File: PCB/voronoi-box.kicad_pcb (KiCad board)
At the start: 2 copper layers, 16 parts, among them J1 Conn_01x02_Male, J2 Conn_01x02_Male, J3 Conn_01x03_Female, SW1 SW_Push, SW2 SW_Push, U1 ATtiny85-20PU

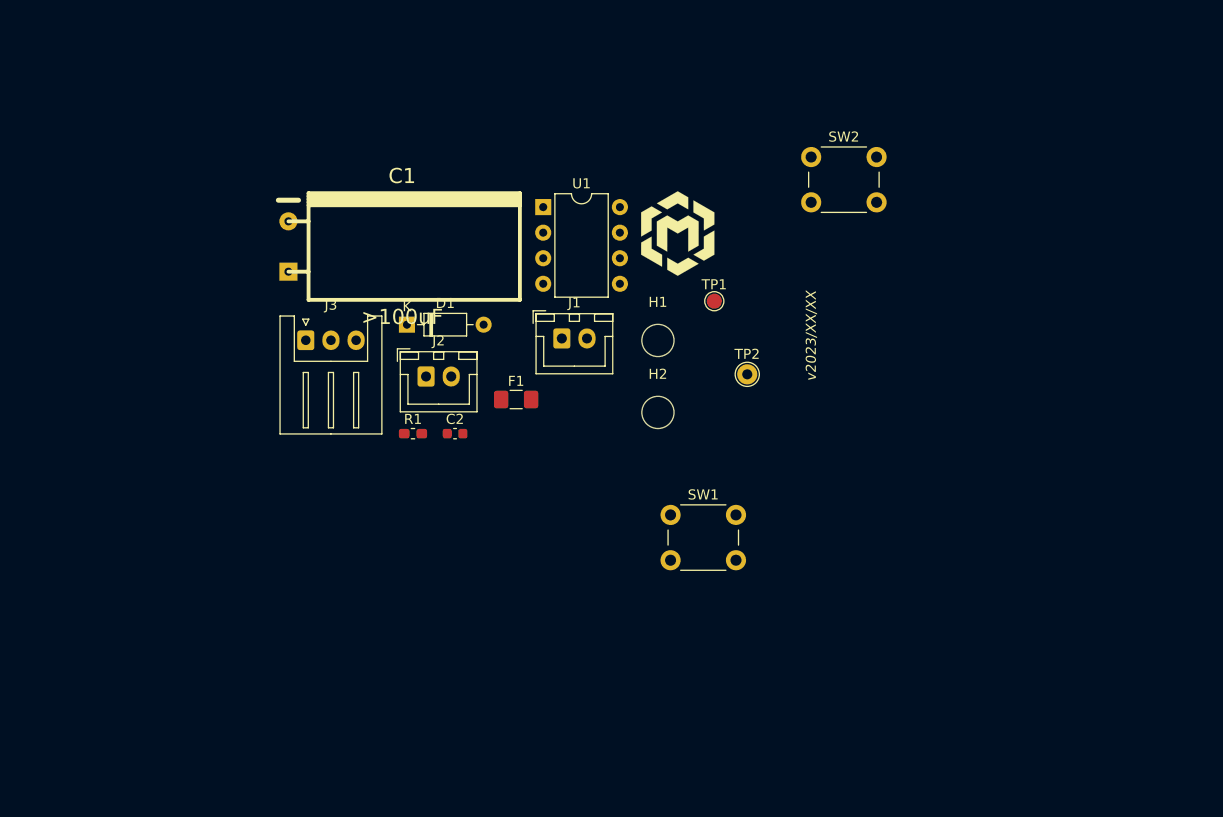
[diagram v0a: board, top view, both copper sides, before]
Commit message: extend Readme with a huge knowledge drop, create new power path with dedicated parts, add ISP, use analog mux for buttons, try to fix CI
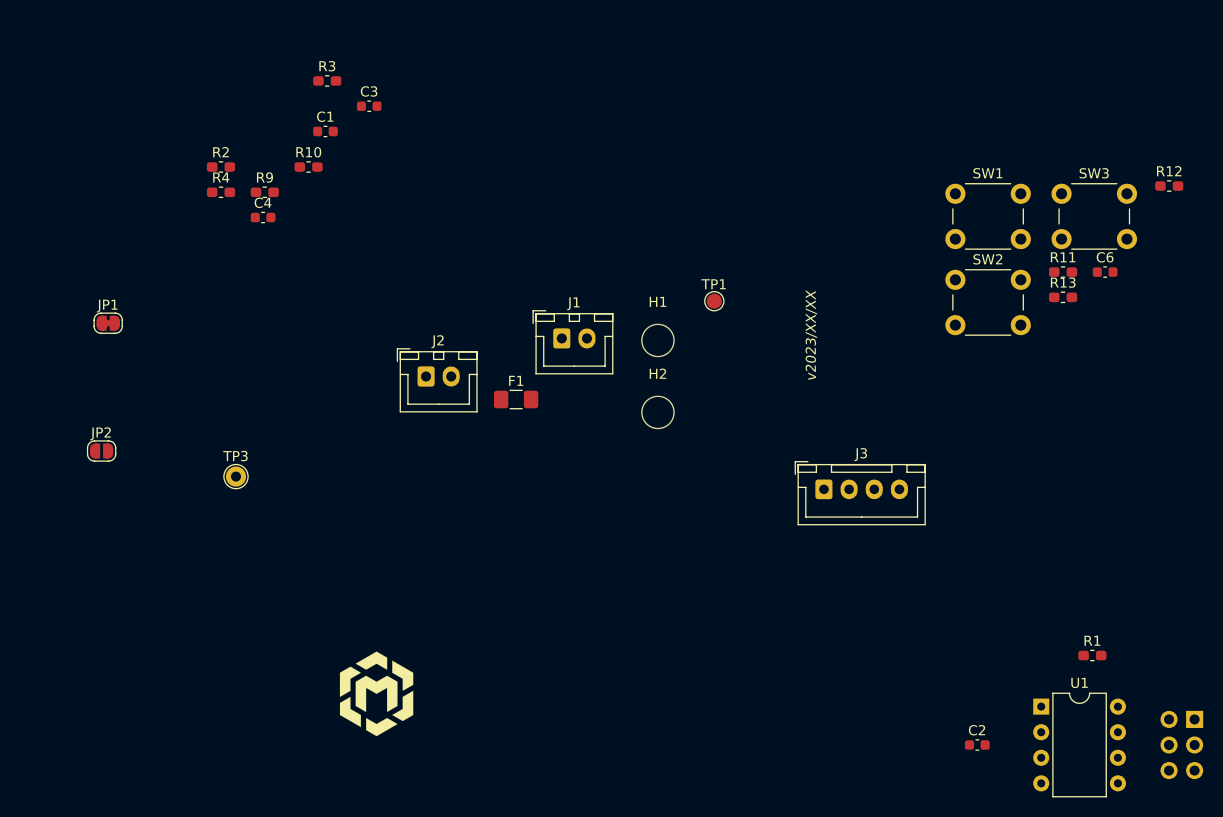
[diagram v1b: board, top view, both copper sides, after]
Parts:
- removed D1: D, Diode_THT:D_DO-35_SOD27_P7.62mm_Horizontal
- removed TP2: RESERVE, TestPoint:TestPoint_THTPad_D2.0mm_Drill1.0mm
- added C3: 1uF, Capacitor_SMD:C_0603_1608Metric, F.Cu at (43.7, 21.6)
- added C4: 100nF, Capacitor_SMD:C_0603_1608Metric, F.Cu at (33.2, 32.7)
- added C6: 100nF, Capacitor_SMD:C_0603_1608Metric, F.Cu at (116.8, 38.1)
- added J4: AVR-ISP-6, Connector_PinHeader_2.54mm:PinHeader_2x03_P2.54mm_Vertical, B.Cu at (125.7, 82.5)
- added JP1: Cut for NTC, Jumper:SolderJumper-2_P1.3mm_Bridged_RoundedPad1.0x1.5mm, F.Cu at (17.8, 43.2)
- added JP2: Join without BMS, Jumper:SolderJumper-2_P1.3mm_Open_RoundedPad1.0x1.5mm, F.Cu at (17.1, 55.9)
- added R10: 1k, Resistor_SMD:R_0603_1608Metric_Pad1.05x0.95mm_HandSolder, F.Cu at (37.7, 27.7)
- added R11: 1k, Resistor_SMD:R_0603_1608Metric_Pad1.05x0.95mm_HandSolder, F.Cu at (112.7, 38.1)
- added R12: 2.2k, Resistor_SMD:R_0603_1608Metric_Pad1.05x0.95mm_HandSolder, F.Cu at (123.2, 29.6)
- added R13: 4.7k, Resistor_SMD:R_0603_1608Metric_Pad1.05x0.95mm_HandSolder, F.Cu at (112.7, 40.6)
- added R2: 2k, Resistor_SMD:R_0603_1608Metric_Pad1.05x0.95mm_HandSolder, F.Cu at (29.0, 27.7)
- added R3: 1.5k, Resistor_SMD:R_0603_1608Metric_Pad1.05x0.95mm_HandSolder, F.Cu at (39.5, 19.1)
- added R4: 10k, Resistor_SMD:R_0603_1608Metric_Pad1.05x0.95mm_HandSolder, F.Cu at (29.0, 30.2)
- added R9: 47k, Resistor_SMD:R_0603_1608Metric_Pad1.05x0.95mm_HandSolder, F.Cu at (33.3, 30.2)
- added SW3: SW_3, Button_Switch_THT:SW_PUSH_6mm_H4.3mm, F.Cu at (112.5, 30.3)
- added TP3: TEMP, TestPoint:TestPoint_THTPad_D2.0mm_Drill1.0mm, F.Cu at (30.5, 58.4)
- C1: value >100uF -> 1uF; footprint w_capacitors:CP_10x20mm_hor -> Capacitor_SMD:C_0603_1608Metric
- J1: value Conn_01x02_Male -> LiPo (1S/3.7V)
- J2: value Conn_01x02_Male -> USB/PWR
- J3: value Conn_01x03_Female -> LEDs; footprint Connector_JST:JST_XH_S3B-XH-A_1x03_P2.50mm_Horizontal -> Connector_JST:JST_XH_B4B-XH-A_1x04_P2.50mm_Vertical
- R1: value 10k -> 4.7k
- SW1: value SW_Push -> SW_1
- SW2: value SW_Push -> SW_2
- moved R1 71.0 mm to (115.6, 76.2)
- moved U1 70.1 mm to (110.5, 81.3)
- moved C2 60.4 mm to (104.1, 85.1)
- moved L1 54.7 mm to (44.5, 80.0)
- moved J3 53.6 mm to (88.9, 59.7)
- moved SW1 42.7 mm to (102.0, 30.3)
- moved SW2 18.8 mm to (102.0, 38.9)
- moved C1 13.7 mm to (39.4, 24.1)
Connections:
- net Net-(R1-Pad2) renamed /RESET
- net Net-(TP1-Pad1) renamed /AREF
- C1 pad 1: VCC -> VBUS
- F1 pad 1: (no net) -> VBUS
- F1 pad 2: VBUS -> Net-(F1-Pad2)
- J1 pad 1: (no net) -> +BATT
- J1 pad 2: GND -> -BATT
- J2 pad 1: VBUS -> Net-(F1-Pad2)
- J3 pad 3: GND -> /D_LEDS2
- SW1 pad 2: /D_mode -> Net-(R11-Pad2)
- SW2 pad 2: /D_brightness -> Net-(R12-Pad2)
- U1 pad 2: Net-(TP2-Pad1) -> /D_switches
- U1 pad 7: /D_mode -> /D_LEDS2

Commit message: add more readme comments and links, add capacitors and more part numbers, fix lib ref
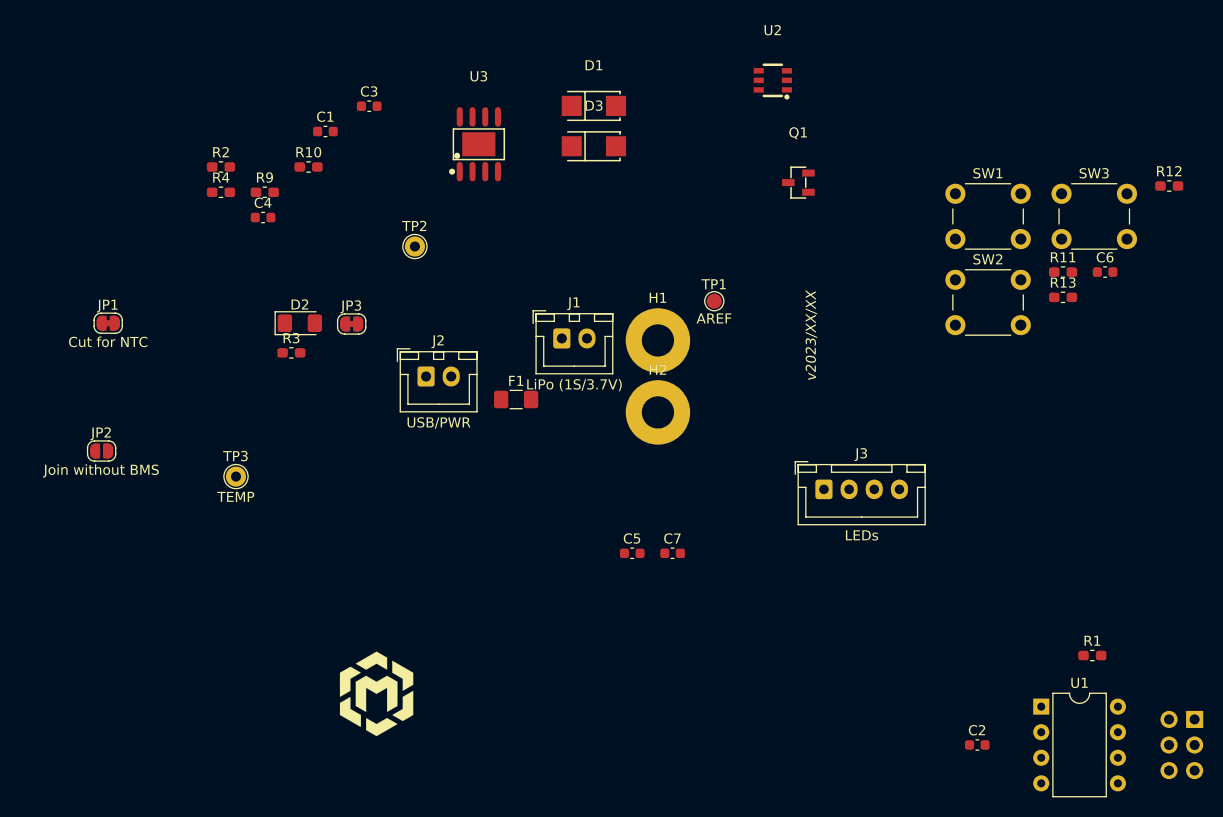
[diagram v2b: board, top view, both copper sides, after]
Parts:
- added C5: 22uF, Capacitor_SMD:C_0603_1608Metric, F.Cu at (69.8, 66.0)
- added C7: 22uF, Capacitor_SMD:C_0603_1608Metric, F.Cu at (73.9, 66.0)
- added D1: SS34_C8678, lcsc:SMA_L4.3-W2.6-LS5.2-RD, F.Cu at (66.0, 21.6)
- added D2: LED, LED_SMD:LED_1206_3216Metric_Pad1.42x1.75mm_HandSolder, F.Cu at (36.8, 43.2)
- added D3: SS34_C8678, lcsc:SMA_L4.3-W2.6-LS5.2-RD, F.Cu at (66.0, 25.6)
- added JP3: Cut for LED, Jumper:SolderJumper-2_P1.3mm_Bridged_RoundedPad1.0x1.5mm, F.Cu at (42.0, 43.3)
- added Q1: AO3415_C181094, lcsc:SOT-23-3_L2.9-W1.3-P1.90-LS2.4-BR, F.Cu at (86.4, 29.2)
- added TP2: PB4, TestPoint:TestPoint_THTPad_D2.0mm_Drill1.0mm, F.Cu at (48.3, 35.6)
- added U2: BQ21040DBVR, lcsc:SOT-23-6_L2.9-W1.6-P0.95-LS2.8-BR, F.Cu at (83.8, 19.1)
- added U3: XB8089D0, lcsc:SOIC-8_L4.9-W3.9-P1.27-LS6.0-BL-EP3.3-1, F.Cu at (54.6, 25.4)
- F1: value 1A -> 1.5A
- H1, H2: footprint MountingHole:MountingHole_3.2mm_M3_DIN965 -> MountingHole:MountingHole_3.2mm_M3_Pad
- J4: value AVR-ISP-6 -> AVR-ISP
- R2: value 2k -> 2.2k
- moved R3 27.3 mm to (36.0, 46.1)
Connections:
- R2 pad 2: (no net) -> Net-(R2-Pad2)
- R3 pad 1: (no net) -> Net-(D2-Pad2)
- U1 pad 3: (no net) -> Net-(JP3-Pad1)
